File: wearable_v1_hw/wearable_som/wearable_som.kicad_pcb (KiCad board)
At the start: 2 copper layers, 40 x 30 mm, 39 parts, among them IC1 TPS7A0228PDBVR, IC2 DA7280-00FV2, J1 Conn_01x04, J2 USB4105-GF-A, M1 Motor_DC, Q1 PMOS, SW1 Reset, SW2 SW_Nidec_CAS-120A1, SW3 Boot, U1 STM32WB55RGVx, U2 BMI270, U3 MCP73831-2-MC, U4 DLF162500LT-5028A1, U5 2450AT18A100E, U6 USBLC6-2SC6, Y1 Crystal_GND23

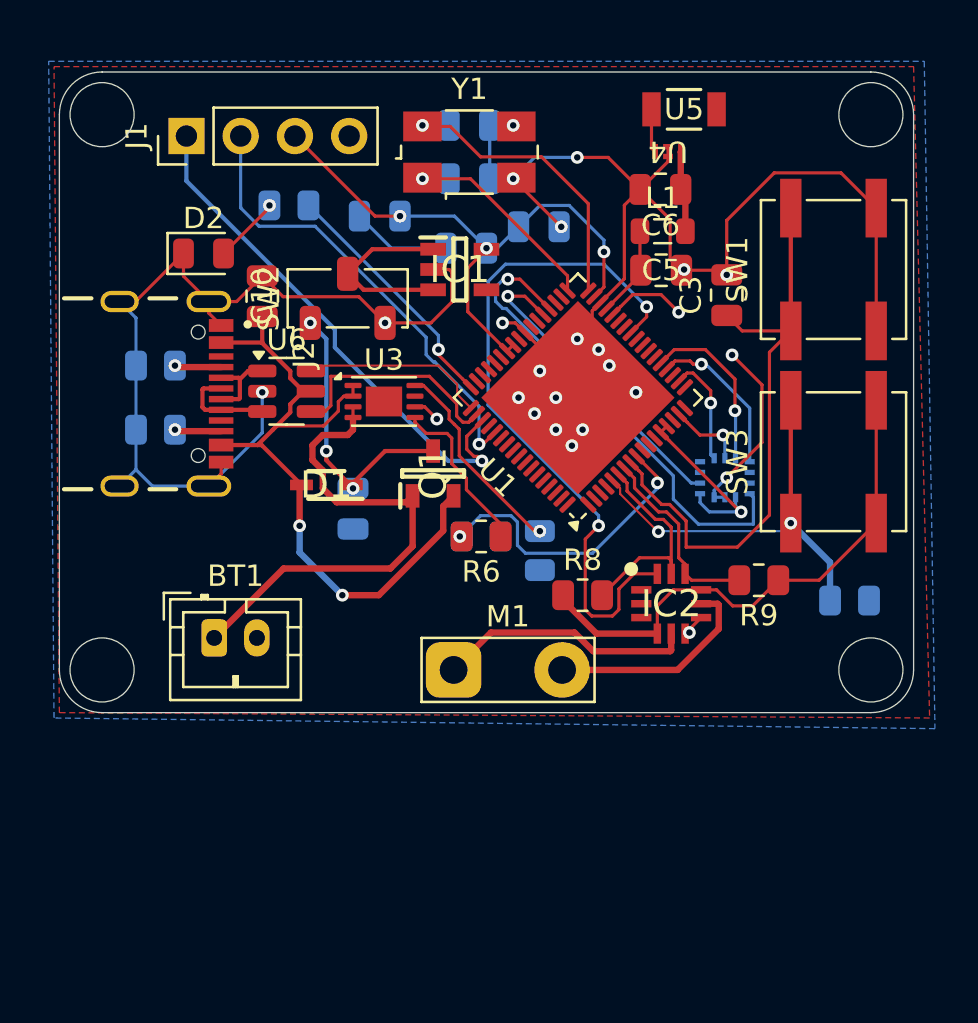
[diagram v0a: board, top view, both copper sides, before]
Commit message: revisions revisions
2->4 layers
improved ground plane + ic placement
added adc for force sensor
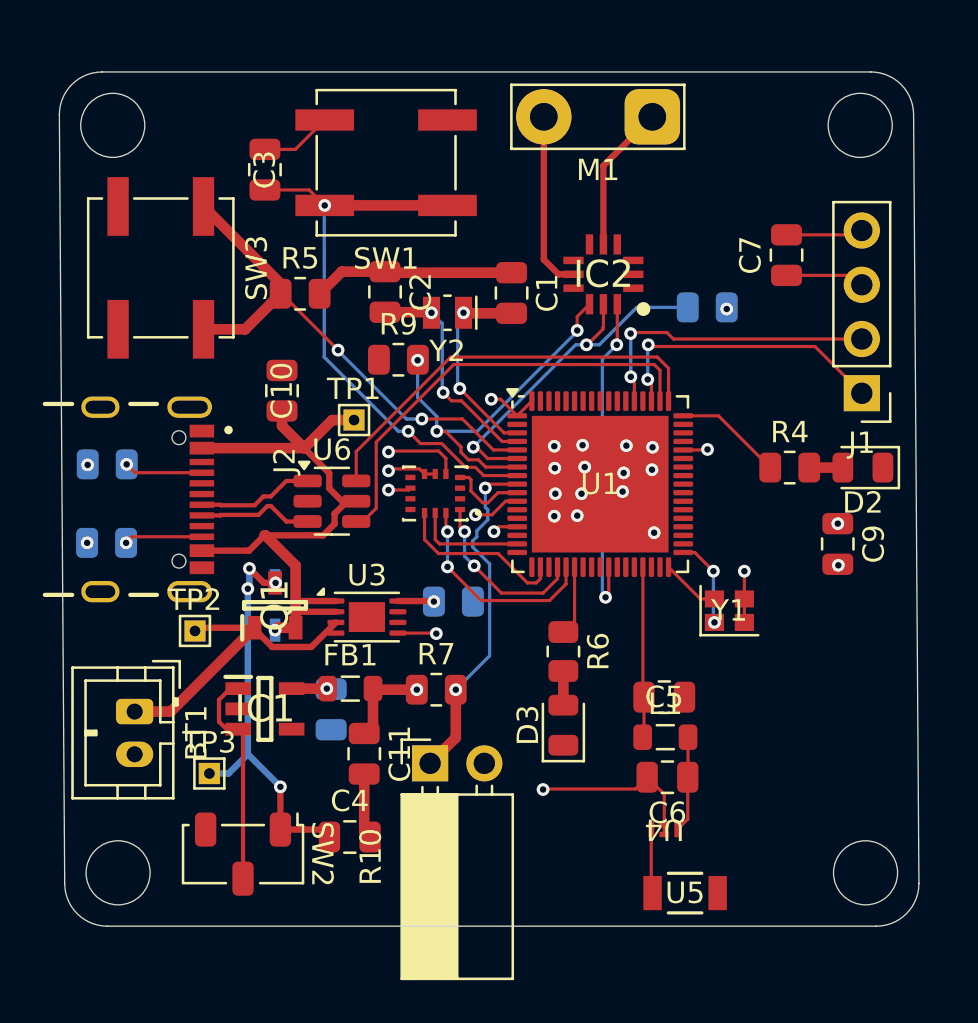
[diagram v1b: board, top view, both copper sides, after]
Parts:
- added C11: 100nF, Capacitor_SMD:C_0805_2012Metric, F.Cu at (108.0, 140.4)
- added D3: LED, LED_SMD:LED_0805_2012Metric, F.Cu at (117.3, 139.1)
- added FB1: FerriteBead, Inductor_SMD:L_0805_2012Metric, F.Cu at (107.4, 137.4)
- added R10: R_Variable, Connector_PinSocket_2.54mm:PinSocket_1x02_P2.54mm_Horizontal, F.Cu at (111.1, 140.9)
- added TP1: TestPoint, TestPoint:TestPoint_THTPad_1.0x1.0mm_Drill0.5mm, F.Cu at (107.5, 124.8)
- added TP2: TestPoint, TestPoint:TestPoint_THTPad_1.0x1.0mm_Drill0.5mm, F.Cu at (100.1, 134.7)
- added TP3: TestPoint, TestPoint:TestPoint_THTPad_1.0x1.0mm_Drill0.5mm, F.Cu at (100.8, 141.3)
- added Y2: Crystal, Crystal:Crystal_SMD_MicroCrystal_CC8V-T1A-2Pin_2.0x1.2mm, F.Cu at (111.9, 119.8)
- C1, C2, C4, C7, C9, R4, R5, R7, U2: moved to F.Cu
- D1, R8: moved to B.Cu
- R6: value 10k -> 4.7k
- Y1: footprint Crystal:Crystal_SMD_0603-4Pin_6.0x3.5mm -> Crystal:Crystal_SMD_2016-4Pin_2.0x1.6mm
- moved U5 36.7 mm to (123.0, 146.9)
- moved J1 33.8 mm to (131.3, 123.5), turned to 180 degrees
- moved SW3 32.8 mm to (98.5, 117.7), turned to -90 degrees
- moved D2 32.5 mm to (131.4, 127.0), turned to 180 degrees
- moved U4 31.7 mm to (122.1, 144.0)
- moved R5 29.5 mm to (105.0, 118.9)
- moved C6 27.5 mm to (122.2, 141.5)
- moved M1 27.5 mm to (121.5, 110.6), turned to 180 degrees
- moved SW2 26.5 mm to (102.3, 145.1), turned to -90 degrees
- moved R4 26.5 mm to (128.0, 127.0), turned to 0 degrees
- moved Y1 24.7 mm to (125.1, 133.7)
- moved C8 24.6 mm to (106.5, 138.3), turned to -90 degrees
- moved L1 23.7 mm to (122.1, 139.7)
- moved IC1 22.5 mm to (103.4, 138.3)
- moved C3 22.4 mm to (103.4, 113.1)
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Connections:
- net /USB_DM renamed /USB_DN
- C1 pad 2: /OSC_IN -> /RCC_OSC32_IN
- C2 pad 2: /OSC_OUT -> /RCC_OSC32_OUT
- R6 pad 1: /STAT -> /LED1
- R6 pad 2: /ADC1_IN1 -> Net-(D3-A)
- R7 pad 1: /ADC1_IN1 -> +3.3VA
- R7 pad 2: GND -> /ADC1_IN1
- U1 pad 10: unconnected-(U1-PC1-Pad10) -> /INT1
- U1 pad 11: unconnected-(U1-PC2-Pad11) -> /INT2
- U1 pad 14: +3.3V -> +3.3VA
- U1 pad 23: unconnected-(U1-PA8-Pad23) -> /LED1
- U1 pad 3: unconnected-(U1-PC14-Pad3) -> /RCC_OSC32_IN
- U1 pad 38: /INT1 -> unconnected-(U1-PB0-Pad38)
- U1 pad 39: /INT2 -> unconnected-(U1-PB1-Pad39)
- U1 pad 4: unconnected-(U1-PC15-Pad4) -> /RCC_OSC32_OUT
- U1 pad 47: unconnected-(U1-PB13-Pad47) -> /STAT
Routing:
- net GND: track 116.8 -> 33.0 mm, vias 24 -> 20
- net +3.3V: track 65.0 -> 11.5 mm
- net /INT1: track 22.5 -> 3.68 mm, vias 1 -> 0
- net /NIRQ: track 32.8 -> 15.6 mm
- net +3.3VA: track 0.00 -> 14.4 mm, vias 0 -> 2
- net /OSC_OUT: track 14.6 -> 2.77 mm, vias 1 -> 0
- net /STAT: track 7.81 -> 19.2 mm, vias 0 -> 2
- net /USB_DN: track 8.69 -> 19.6 mm
- net /SWDIO: track 24.5 -> 13.7 mm, vias 1 -> 2
- net /RCC_OSC32_OUT: track 0.00 -> 10.6 mm, vias 0 -> 2
- net /USB_DP: track 10.7 -> 20.6 mm
- net /RCC_OSC32_IN: track 0.00 -> 9.51 mm, vias 0 -> 2
- net /ICS1_SDA: track 8.99 -> 18.3 mm, vias 0 -> 3
- net /VBAT+: track 23.5 -> 14.8 mm
- net Net-(U3-PROG): track 9.62 -> 1.70 mm
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- added copper zone on In1.Cu, net +3.3V
- added copper zone on In2.Cu, net GND
- removed copper zone on F.Cu, net +3.3V
- removed copper zone on B.Cu, net GND
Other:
- board size 40 x 30 mm -> 40.2 x 40 mm
- copper layers 2 -> 4

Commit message: fix drc errors
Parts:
- moved R3 3.88 mm to (108.7, 131.6), turned to 180 degrees
- moved U1 1.12 mm to (120.2, 127.8)
- moved Y1 1.00 mm to (126.1, 133.8)
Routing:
- net GND: track 33.0 -> 60.9 mm, vias 20 -> 35
- net +3.3V: track 11.5 -> 23.7 mm, vias 5 -> 15
- net /DN: track 5.43 -> 8.66 mm
- net /DP: track 5.43 -> 7.97 mm
- net /NIRQ: track 15.6 -> 18.0 mm
- net /SWCLK: track 14.2 -> 16.2 mm
- net /STAT: track 19.2 -> 21.0 mm
- net /NRST: track 27.3 -> 29.0 mm
- net /SPI1_SCK: track 5.17 -> 6.42 mm
- net /INT2: track 7.83 -> 9.08 mm
- net /USB_DP: track 20.6 -> 21.8 mm
- net /INT1: track 3.68 -> 4.80 mm
- net Net-(U1-PH3): track 24.0 -> 25.1 mm
- net /USB_DN: track 19.6 -> 20.7 mm
- net /RCC_OSC32_OUT: track 10.6 -> 11.7 mm
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
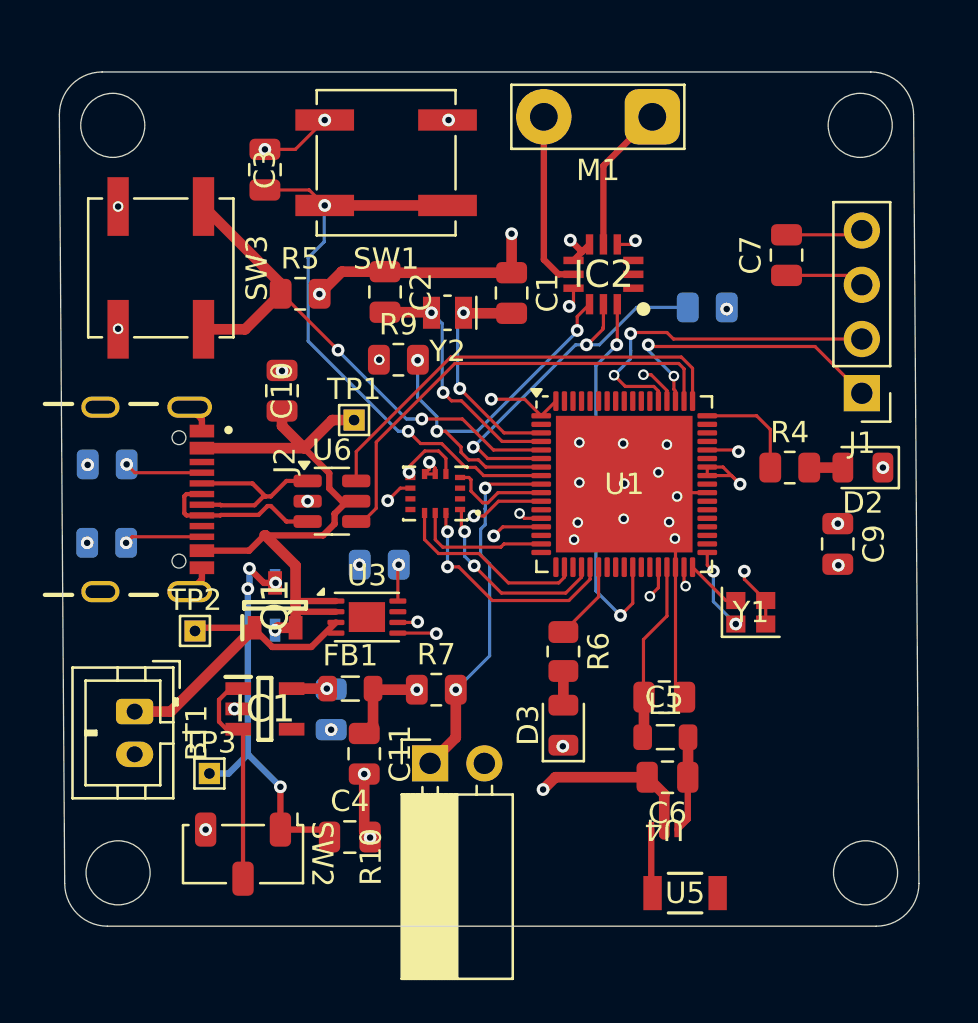
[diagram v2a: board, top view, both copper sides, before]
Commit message: final v1 layout done
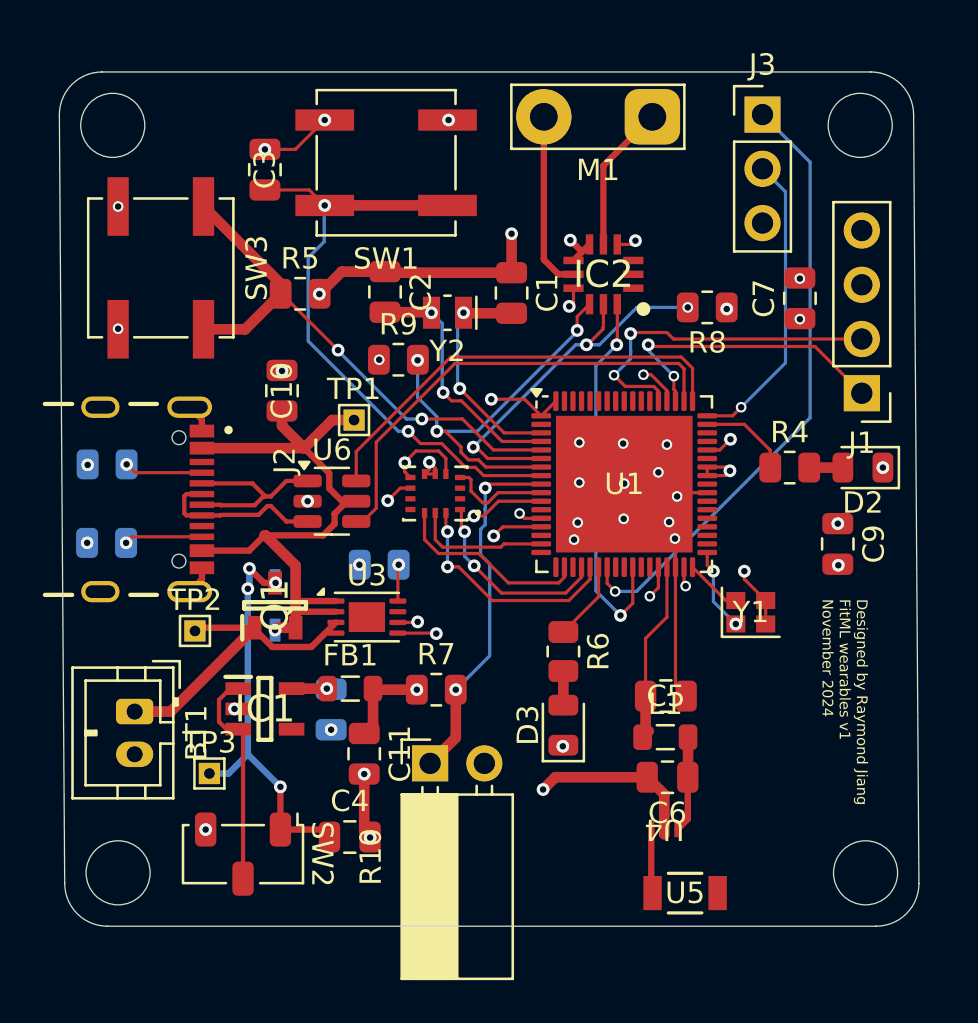
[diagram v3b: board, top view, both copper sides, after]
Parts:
- added J3: Conn_01x03, Connector_PinHeader_2.54mm:PinHeader_1x03_P2.54mm_Vertical, F.Cu at (126.7, 110.5)
- R8: moved to F.Cu
- moved C7 2.12 mm to (128.4, 119.1)
- moved C5 0.09 mm to (122.2, 137.7)
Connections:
- U1 pad 24: unconnected-(U1-PA9-Pad24) -> /USART1_TX
- U1 pad 50: unconnected-(U1-PC6-Pad50) -> /LED0
- U1 pad 51: /LED0 -> /USART1_RX
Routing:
- net /USART1_TX: track 0.00 -> 28.9 mm, vias 0 -> 1
- net /USART1_RX: track 0.00 -> 14.2 mm, vias 0 -> 1
- net GND: track 60.9 -> 56.8 mm, vias 35 -> 36
- net +3.3V: track 23.7 -> 19.8 mm, vias 15 -> 16
- net /LED0: track 5.00 -> 4.26 mm
- net /ICS1_SCL: vias 2 -> 3
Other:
- board text added: "Designed by Raymond Jiang FitML wearables v1 November 2024"

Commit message: wearables v2
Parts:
- C11: value 100nF -> 0.1uF
- C3: value 0.1u -> 0.1uF
- C4: value 1uF -> 0.1uF
